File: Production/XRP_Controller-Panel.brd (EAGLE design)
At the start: 147.6 x 122.7 mm, 610 parts, among them J1 POWER_JACKPOWER_JACK_SLOT, J10 JST_6_PIN_VERTICAL, J11 JST_6_PIN_VERTICAL, J12 Vertical Qwiic Connector, J13 Vertical Qwiic Connector, J14 Vertical Qwiic Connector, J15 JST_6_PIN_VERTICAL, J18 Vertical Qwiic Connector, J19 Vertical Qwiic Connector, J2 JST_6_PIN_VERTICAL, J20 Vertical Qwiic Connector, J21 Vertical Qwiic Connector, J22 POWER_JACKPOWER_JACK_SLOT, J23 JST_6_PIN_VERTICAL, J24 JST_6_PIN_VERTICAL, J25 JST_6_PIN_VERTICAL, J26 JST_6_PIN_VERTICAL, J29 Vertical Qwiic Connector, J3 JST_6_PIN_VERTICAL, J30 Vertical Qwiic Connector, J31 Vertical Qwiic Connector, J32 Vertical Qwiic Connector, J33 POWER_JACKPOWER_JACK_SLOT, J34 JST_6_PIN_VERTICAL, J35 JST_6_PIN_VERTICAL, J36 JST_6_PIN_VERTICAL, J37 JST_6_PIN_VERTICAL, J4 JST_6_PIN_VERTICAL, J40 Vertical Qwiic Connector, J41 Vertical Qwiic Connector, J42 Vertical Qwiic Connector, J43 Vertical Qwiic Connector, J44 POWER_JACKPOWER_JACK_SLOT, J5 JST_6_PIN_VERTICAL, J6 JST_6_PIN_VERTICAL, J9 Vertical Qwiic Connector, Q12 20V/4.2A/52mΩ/1.4W, Q13 20V/4.2A/52mΩ/1.4W, Q15 20V/4.2A/52mΩ/1.4W, Q16 20V/4.2A/52mΩ/1.4W, Q19 20V/4.2A/52mΩ/1.4W, Q20 20V/4.2A/52mΩ/1.4W, Q22 20V/4.2A/52mΩ/1.4W, Q23 20V/4.2A/52mΩ/1.4W, Q26 20V/4.2A/52mΩ/1.4W, Q27 20V/4.2A/52mΩ/1.4W, Q3 20V/4.2A/52mΩ/1.4W, Q4 20V/4.2A/52mΩ/1.4W, Q5 20V/4.2A/52mΩ/1.4W, Q6 20V/4.2A/52mΩ/1.4W, Q8 20V/4.2A/52mΩ/1.4W, Q9 20V/4.2A/52mΩ/1.4W, U1 RPI_PICO_W, U10 AP63357, U11 LSM6DS0, U12 DRV8835, U13 DRV8835, U14 RPI_PICO_W, U15 AP63357, U16 LSM6DS0, U17 DRV8835, U18 DRV8835, U19 RPI_PICO_W, U2 AP63357, U20 AP63357, U3 LSM6DS0, U4 LSM6DS0, U5 DRV8835, U6 DRV8835, U7 DRV8835, U8 DRV8835, U9 RPI_PICO_W

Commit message: Add v09 panel files
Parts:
- removed C31, C34, C35, C36, C38, C42, C43, C44, C45, C48, C49, C50, C52, C56: 0.1uF, SparkFun-Capacitors:0603
- removed C32, C33, C46, C47: 100uF, SparkFun-Capacitors:PANASONIC_D
- removed C37, C51: 10uF, SparkFun-Capacitors:0805
- removed C39, C53: 47pF, SparkFun-Capacitors:0603
- removed C40, C41, C54, C55: 22uF, SparkFun-Capacitors:0805
- removed F3, F4: 16V/2.5A(5A TRIP), SparkFun-Fuses:1812
- removed FD10, FD11, FD12, FD13, FD14, FD15, FD16, FD9: FIDUCIAL1X2, SparkFun-Aesthetics:FIDUCIAL-1X2
- removed H10, H11, H12, H13, H14, H15, H16, H9: STAND-OFF, SparkFun-Hardware:STAND-OFF
- removed I2C2, I2C3: JUMPER-SMT_3_2-NC_TRACE_SILK, SparkFun-Jumpers:SMT-JUMPER_3_2-NC_TRACE_SILK
- removed IMU_ADR2, IMU_ADR3, USB_POW, USB_POW1, USB_POW2, USB_POW3: JUMPER-SMT_2_NO_SILK, SparkFun-Jumpers:SMT-JUMPER_2_NO_SILK
- removed J23, J24, J25, J26, J34, J35, J36, J37: JST_6_PIN_VERTICAL, SparkFun-Connectors:JST-6-SMD-VERT-1.0MM
- removed J27, J28, J38, J39: (no value), SparkFun-Connectors:1X03_NO_SILK
- removed J29, J30, J31, J32, J40, J41, J42, J43: Vertical Qwiic Connector, SparkFun-Connectors:JST04_1MM_VERT
- removed J33, J44: POWER_JACKPOWER_JACK_SLOT, SparkFun-Connectors:POWER_JACK_PTH_SLOT
- removed L3, L4: 6.8UH, Buck5V:07A7_6U8H
- removed LOGO10, LOGO14: QWIIC_LOGO_5MM, SparkFun-Aesthetics:QWIIC_5MM
- removed LOGO11, LOGO12, LOGO15, LOGO16, LOGO7, LOGO8: SFE_LOGO_NAME_FLAME.1_INCH, SparkFun-Aesthetics:SFE_LOGO_NAME_FLAME_.1
- removed LOGO13, LOGO9: OSHW-LOGOS, SparkFun-Aesthetics:OSHW-LOGO-S
- removed MOT_MODE_L1, MOT_MODE_L3, MOT_MODE_R1, MOT_MODE_R3, PWR, PWR1, PWR2, PWR3: JUMPER-SMT_2_NC_TRACE_SILK, SparkFun-Jumpers:SMT-JUMPER_2_NC_TRACE_SILK
- removed Q15, Q16, Q19, Q20, Q22, Q23, Q26, Q27: 20V/4.2A/52mΩ/1.4W, SparkFun-DiscreteSemi:SOT23-3
- removed Q17, Q18, Q21, Q24, Q25, Q28: (no value), SparkFun-DiscreteSemi:SOT363_PHILIPS
- removed R41, R46, R49, R50, R53, R54, R55: 100k, SparkFun-Resistors:0603
- removed R42, R51, R52, R56: 1M, SparkFun-Resistors:0603
- removed R43: 1k, SparkFun-Resistors:0603
- removed R44, R45: 2.2k, SparkFun-Resistors:0603
- removed R47: 180k, SparkFun-Resistors:0603
- removed R48: 33k, SparkFun-Resistors:0603
- removed RESET2, RESET3: MOMENTARY-SWITCH-SPST-SMD-4.6X2.8MM, SparkFun-Switches:TACTILE_SWITCH_SMD_4.6X2.8MM
- removed S3, S4: (no value), SparkFun-Switches:SWITCH_SPST_SMD_A
- removed U$193, U$267: (no value), output:#I2C#0
- removed U$194, U$268: (no value), output:ON0
- removed U$195, U$269: (no value), output:OFF0
- removed U$196, U$270: (no value), output:X0
- removed U$197, U$271: (no value), output:Y0
- removed U$198, U$272: (no value), output:Z0
- removed U$199, U$273: (no value), output:#IMU_ADR#0
- removed U$200, U$274: (no value), output:#USB_POW#0
- removed U$201, U$275: (no value), output:#MOT_MODE_R#0
- removed U$202, U$276: (no value), output:#MOT_MODE_L#0
- removed U$203, U$277: (no value), output:#PWR_LED#0
- removed U$204, U$206, U$278, U$280: (no value), output:XRP_ROBOT0
- removed U$205, U$207, U$279, U$281: (no value), output:CONTROLLER0
- removed U$208, U$282: (no value), output:#RANGE#0
- removed U$209, U$283: (no value), output:#LINE#0
- removed U$210, U$284: (no value), output:#MOTOR_L#0
- removed U$211, U$285: (no value), output:#MOTOR_3#0
- removed U$212, U$286: (no value), output:#SERVO_1#0
- removed U$213, U$287: (no value), output:#MOTOR_R#0
- removed U$214, U$288: (no value), output:#MOTOR_4#0
- removed U$215, U$289: (no value), output:#SERVO_2#0
- removed U$216, U$290: (no value), output:#11V_MAX###0
- removed U$217, U$291: (no value), output:#MLP#0
- removed U$218, U$292: (no value), output:#MLN#0
- removed U$219, U$293: (no value), output:#M3N#0
- removed U$220, U$294: (no value), output:#M3P#0
- removed U$221, U$295: (no value), output:#MRN#0
- removed U$222, U$296: (no value), output:#MRP#0
- removed U$223: (no value), output:#POWER#0
- removed U$224: (no value), output:PWR0
- removed U$225: (no value), output:RESET0
- removed U$226: (no value), output:#CONN4#0
- removed U$227, U$233, U$257, U$259, U$261: (no value), output:#GND#0
- removed U$228, U$234, U$258, U$260: (no value), output:#3V3#0
- removed U$229: (no value), output:#IO0#0
- removed U$230: (no value), output:#IO1#0
- removed U$231: (no value), output:#IO5#0
- removed U$232: (no value), output:#IO4#0
- removed U$235: (no value), output:#IO8#0
- removed U$236: (no value), output:#IO9#0
- removed U$237, U$239, U$247, U$249, U$264: (no value), output:#GND#10
- removed U$238, U$240, U$248, U$250: (no value), output:#3V3#4
- removed U$241: (no value), output:#IO12#0
- removed U$242: (no value), output:#IO13#0
- removed U$243: (no value), output:#M4P#0
- removed U$244: (no value), output:#M4N#0
- removed U$245: (no value), output:#IO27#0
- removed U$246: (no value), output:#IO28#0
- removed U$251: (no value), output:#IO26#0
- removed U$252: (no value), output:#IO22#0
- removed U$253: (no value), output:#IO18#0
- removed U$254: (no value), output:#IO19#0
- removed U$255: (no value), output:#IO20#0
- removed U$256: (no value), output:#IO21#0
- removed U$262: (no value), output:#5V#0
- removed U$263: (no value), output:#IO16#0
- removed U$265: (no value), output:#IO17#0
- removed U$266: (no value), output:#5V#18
- removed U11, U16: LSM6DS0, SparkFun-Sensors:LGA14L
- removed U12, U13, U17, U18: DRV8835, SparkFun-IC-Special-Function:WSON-12
- removed U14, U19: RPI_PICO_W, RPI_PICO_W:RPI_PICO_W
- removed U15, U20: AP63357, Buck5V:V-DFN3020-13
- added MOT_PWR, MOT_PWR1, SYS_PWR, SYS_PWR1, USER_BTN, USER_BTN1, VIN_MEAS, VIN_MEAS1, VUSB, VUSB1: JUMPER-SMT_2_NC_TRACE_SILK, SparkFun-Jumpers:SMT-JUMPER_2_NC_TRACE_SILK
- added TP13, TP14, TP15, TP16, TP17, TP18, TP19, TP20, TP21, TP22, TP23, TP24, TP25, TP26, TP27, TP28, TP29, TP30, TP31, TP32, TP33, TP34, TP35, TP36, TP37, TP38, TP39, TP40, TP41, TP42, TP43, TP44, TP45, TP46, TP47, TP48, TP49, TP50, TP51, TP52, TP53, TP54, TP55, TP56, TP57, TP58, TP59, TP60, TP61, TP62, TP63, TP64, TP65, TP66, TP67, TP68, TP69, TP70, TP71, TP72, TP73, TP74, TP75, TP76, TP77, TP78: TEST-POINT3X5, SparkFun-Connectors:PAD.03X.05
- added USER, USER1: MOMENTARY-SWITCH-SPST-SMD-4.6X2.8MM, SparkFun-Switches:TACTILE_SWITCH_SMD_4.6X2.8MM
- C18: value 100uF -> 0.1uF; device SparkFun-Capacitors:PANASONIC_D -> SparkFun-Capacitors:0603
- C20: value 0.1uF -> 100uF; device SparkFun-Capacitors:0603 -> SparkFun-Capacitors:PANASONIC_D
- C23: value 10uF -> 0.1uF; device SparkFun-Capacitors:0805 -> SparkFun-Capacitors:0603
- C24: value 0.1uF -> 10uF; device SparkFun-Capacitors:0603 -> SparkFun-Capacitors:0805
- C25: value 47pF -> 0.1uF
- C26: value 22uF -> 47pF; device SparkFun-Capacitors:0805 -> SparkFun-Capacitors:0603
- C28: value 0.1uF -> 22uF; device SparkFun-Capacitors:0603 -> SparkFun-Capacitors:0805
- IMU_ADR, IMU_ADR1: value JUMPER-SMT_2_NO_SILK -> JUMPER-SMT_2_NC_TRACE_SILK; device SparkFun-Jumpers:SMT-JUMPER_2_NO_SILK -> SparkFun-Jumpers:SMT-JUMPER_2_NC_TRACE_SILK
- J16, J17, J7, J8: device SparkFun-Connectors:1X03_NO_SILK -> SparkFun-Connectors:1X03_LOCK_NO_SILK
- LOGO2: value QWIIC_LOGO_5MM -> OSHW-LOGOS; device SparkFun-Aesthetics:QWIIC_5MM -> SparkFun-Aesthetics:OSHW-LOGO-S
- LOGO3: value SFE_LOGO_NAME_FLAME.1_INCH -> SFE_LOGO_NAME_FLAME.3_INCH; device SparkFun-Aesthetics:SFE_LOGO_NAME_FLAME_.1 -> SparkFun-Aesthetics:SFE_LOGO_NAME_FLAME_.3
- LOGO5: value OSHW-LOGOS -> SFE_LOGO_NAME_FLAME.3_INCH; device SparkFun-Aesthetics:OSHW-LOGO-S -> SparkFun-Aesthetics:SFE_LOGO_NAME_FLAME_.3
- LOGO6: value QWIIC_LOGO_5MM -> SFE_LOGO_NAME_FLAME.1_INCH; device SparkFun-Aesthetics:QWIIC_5MM -> SparkFun-Aesthetics:SFE_LOGO_NAME_FLAME_.1
- R15: value 1k -> 33k
- R16, R17, R31: value 2.2k -> 100k
- R18, R39: value 100k -> 10; device SparkFun-Resistors:0603 -> SparkFun-Resistors:1206
- R19: value 180k -> 10; device SparkFun-Resistors:0603 -> SparkFun-Resistors:1206
- R20: value 33k -> 10k
- R21: value 100k -> 4.7k
- R22: value 100k -> 2.2k
- R23: value 1M -> 2.2k
- R24, R28, R37: value 1M -> 100k
- R25: value 100k -> 180k
- R26, R36: value 100k -> 33k
- R29: value 1k -> 1M
- R30: value 2.2k -> 1M
- R33: value 180k -> 100k
- R34: value 33k -> 1M
- R38: value 1M -> 10; device SparkFun-Resistors:0603 -> SparkFun-Resistors:1206
- R40: value 100k -> 10k
- R8: value 1k -> 4.7k
- U$100: device output:#3V3#4 -> output:#GND#0
- U$101: device output:#GND#10 -> output:#3V3#0
- U$102: device output:#3V3#4 -> output:#IO0#0
- U$103: device output:#IO26#0 -> output:#IO1#0
- U$104: device output:#IO22#0 -> output:#IO5#0
- U$105: device output:#IO18#0 -> output:#IO4#0
- U$106: device output:#IO19#0 -> output:#GND#0
- U$107: device output:#IO20#0 -> output:#3V3#0
- U$108: device output:#IO21#0 -> output:#IO8#0
- U$109: device output:#GND#0 -> output:#IO9#0
- U$110, U$112: device output:#3V3#0 -> output:#GND#10
- U$111, U$113: device output:#GND#0 -> output:#3V3#4
- U$114: device output:#5V#0 -> output:#IO12#0
- U$115: device output:#IO16#0 -> output:#IO13#0
- U$116: device output:#GND#10 -> output:#M4P#0
- U$117: device output:#IO17#0 -> output:#M4N#0
- U$118: device output:#5V#18 -> output:#IO27#0
- U$119: device output:#I2C#0 -> output:#IO28#0
- U$120: device output:ON0 -> output:#GND#10
- U$121: device output:OFF0 -> output:#3V3#4
- U$122: device output:X0 -> output:#GND#10
- U$123: device output:Y0 -> output:#3V3#4
- U$124: device output:Z0 -> output:#IO26#0
- U$125: device output:#IMU_ADR#0 -> output:#IO22#0
- U$126: device output:#USB_POW#0 -> output:#IO18#0
- U$127: device output:#MOT_MODE_R#0 -> output:#IO19#0
- U$128: device output:#MOT_MODE_L#0 -> output:#IO20#0
- U$129: device output:#PWR_LED#0 -> output:#IO21#0
- U$13: device output:#CONN4#0 -> output:#VIN_MEAS#0
- U$130, U$132: device output:XRP_ROBOT0 -> output:#GND#0
- U$131, U$133: device output:CONTROLLER0 -> output:#3V3#0
- U$134: device output:#RANGE#0 -> output:#GND#0
- U$135: device output:#LINE#0 -> output:#5V#0
- U$136: device output:#MOTOR_L#0 -> output:#IO16#0
- U$137: device output:#MOTOR_3#0 -> output:#GND#10
- U$138: device output:#SERVO_1#0 -> output:#IO17#0
- U$139: device output:#MOTOR_R#0 -> output:#5V#18
- U$140: device output:#MOTOR_4#0 -> output:#I2C#0
- U$141: device output:#SERVO_2#0 -> output:ON0
- U$142: device output:#11V_MAX###0 -> output:OFF0
- U$143: device output:#MLP#0 -> output:X0
- U$144: device output:#MLN#0 -> output:Y0
- U$145: device output:#M3N#0 -> output:Z0
- U$146: device output:#M3P#0 -> output:#IMU_ADR#0
- U$147: device output:#MRN#0 -> output:#LINE#0
- U$148: device output:#MRP#0 -> output:#MOTOR_L#0
- U$149: device output:#POWER#0 -> output:#MOTOR_3#0
- U$150: device output:PWR0 -> output:#SERVO_1#0
- U$151: device output:RESET0 -> output:#MOTOR_R#0
- U$152: device output:#CONN4#0 -> output:#MOTOR_4#0
- U$153: device output:#GND#0 -> output:#SERVO_2#0
- U$154: device output:#3V3#0 -> output:#11V_MAX###0
- U$155: device output:#IO0#0 -> output:#MLP#0
- U$156: device output:#IO1#0 -> output:#MLN#0
- U$157: device output:#IO5#0 -> output:#M3N#0
- U$158: device output:#IO4#0 -> output:#M3P#0
- U$159: device output:#GND#0 -> output:#MRN#0
- U$160: device output:#3V3#0 -> output:#MRP#0
- U$161: device output:#IO8#0 -> output:#5V_#0
- U$162: device output:#IO9#0 -> output:#GND_#0
- U$163: device output:#GND#10 -> output:#IO16_#0
- U$164: device output:#3V3#4 -> output:#_GND#0
- U$165: device output:#GND#10 -> output:#_5V#0
- U$166: device output:#3V3#4 -> output:#_IO17#0
- U$167: device output:#IO12#0 -> SparkFun-Aesthetics:POLARITY_MARKING_CENTER_POSITIVE#JPG
- U$168: device output:#IO13#0 -> output:X0
- U$169: device output:#M4P#0 -> output:Y0
- U$170: device output:#M4N#0 -> output:Z0
- U$171: device output:#IO27#0 -> output:#EXTRA#0
- U$172: device output:#IO28#0 -> output:#VIN_MEAS#0
- U$173: device output:#GND#10 -> output:USER0
- U$174: device output:#3V3#4 -> output:#USER_BTN#0
- U$175: device output:#GND#10 -> output:0X6B0
- U$176: device output:#3V3#4 -> output:0X6A0
- U$177: device output:#IO26#0 -> output:OPEN#0
- U$178: device output:#IO22#0 -> output:CLOSED#0
- U$179: device output:#IO18#0 -> XRP_LOGOS:XRP_FULL_LOGO
- U$180: device output:#IO19#0 -> output:#VUSB#0
- U$181: device output:#IO20#0 -> XRP_LOGOS:XRP_LOGO
- U$182: device output:#IO21#0 -> output:IO220
- U$183: device output:#GND#0 -> output:#RANGE#0
- U$184: device output:#3V3#0 -> output:#MOT_MODE_R#4#0
- U$185: device output:#GND#0 -> output:#MOT_MODE_L#3#0
- U$186: device output:#3V3#0 -> output:SYS0
- U$187: device output:#GND#0 -> output:MOT0
- U$188: device output:#5V#0 -> output:#MOT#0
- U$189: device output:#IO16#0 -> output:#SYS#0
- U$190: device output:#GND#10 -> output:#PWR#0
- U$191: device output:#IO17#0 -> XRP_COMPONENTS:OPENSTEM_LOGO
- U$192: value (none) -> QWIIC_LOGO; device output:#5V#18 -> XRP_COMPONENTS:QWIIC_INVERTED
- U$26: device output:#POWER#0 -> output:#GND_#0
- U$27: device output:PWR0 -> output:#5V_#0
- U$61: device output:RESET0 -> output:#IO16_#0
- U$65: device output:#USB_POW#0 -> XRP_LOGOS:XRP_LOGO
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- renumbered MOT_MODE_L to MOT_MODE_L/3, MOT_MODE_L2 to MOT_MODE_L/1, MOT_MODE_R to MOT_MODE_R/4, MOT_MODE_R2 to MOT_MODE_R/1
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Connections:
- net N$12 renamed V_SYS
- net N$17 renamed V_POW
- removed net !POW_EN!2: R40.1, S3.2
- removed net !POW_EN!3: R54.1, S4.2
- removed net !RP_RESET!2: C42.1, RESET2.3, RESET2.4, U14.30
- removed net !RP_RESET!3: C56.1, RESET3.3, RESET3.4, U19.30
- removed net 3.3V2: C29.1, C30.1, C31.1, C34.1, D3.A, I2C2.2, J23.3, J24.3, J25.3, J26.3, J29.2, J30.2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
- removed net 3.3V3: C43.1, C44.1, C45.1, C48.1, D4.A, I2C3.2, J34.3, J35.3, J36.3, J37.3, J40.2, J41.2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
- removed net 5V2: C39.1, C40.1, C41.1, J27.2, J28.2, L3.P$2, Q20.3, Q21.1, R33.2
- removed net 5V3: C53.1, C54.1, C55.1, J38.2, J39.2, L4.P$2, Q27.3, Q28.1, R47.2
- removed net 5V_EN2: TP7.1, U15.P$2
- removed net 5V_EN3: TP10.1, U20.P$2
- removed net 5V_PG2: TP8.1, U15.P$5
- removed net 5V_PG3: TP11.1, U20.P$5
- removed net BOOTSEL2: TP9.1, U14.46
- removed net BOOTSEL3: TP12.1, U19.46
- removed net FB2: C39.2, R33.1, R34.2, U15.P$3
- removed net FB3: C53.2, R47.1, R48.2, U20.P$3
- removed net GND2: C29.2, C30.2, C31.2, C32.-, C33.-, C34.2, C35.2, C36.2, C37.2, C40.2, C41.2, C42.2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
- removed net GND3: C43.2, C44.2, C45.2, C46.-, C47.-, C48.2, C49.2, C50.2, C51.2, C54.2, C55.2, C56.2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
- removed net MOT_3_N2: J23.2, U12.5
- removed net MOT_3_N3: J34.2, U17.5
- removed net MOT_3_P2: J23.1, U12.4
- removed net MOT_3_P3: J34.1, U17.4
- removed net MOT_4_N2: J26.2, U13.3
- removed net MOT_4_N3: J37.2, U18.3
- removed net MOT_4_P2: J26.1, U13.2
- removed net MOT_4_P3: J37.1, U18.2
- removed net MOT_L_N2: J24.2, U12.3
- removed net MOT_L_N3: J35.2, U17.3
- removed net MOT_L_P2: J24.1, U12.2
- removed net MOT_L_P3: J35.1, U17.2
- removed net MOT_R_N2: J25.2, U13.5
- removed net MOT_R_N3: J36.2, U18.5
- removed net MOT_R_P2: J25.1, U13.4
- removed net MOT_R_P3: J36.1, U18.4
- removed net N$36 (its old number): Q13.2, Q14.4, U9.39
- removed net N$45: I2C2.1, R31.1
- removed net N$46: C38.1, U15.P$6
- removed net N$47: Q17.2, Q17.5, Q17.6, R35.2
- removed net N$48: Q15.1, Q17.3, R37.2
- removed net N$49: Q18.2, Q18.5, Q18.6, R36.2
- removed net N$50: Q16.1, Q18.3, R38.2
- removed net N$51: Q16.3, Q18.1, USB_POW2.2
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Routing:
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- added copper zone on layer 1, net V_POW
- added copper zone on layer 1, net V_POW1
- removed copper zone on layer 1, net 3.3V2
- removed copper zone on layer 1, net 3.3V3
- removed copper zone on layer 1, net 5V2
- removed copper zone on layer 16, net 5V2
- removed copper zone on layer 1, net 5V3
- removed copper zone on layer 16, net 5V3
- removed copper zone on layer 1, net FB2
- removed copper zone on layer 1, net FB3
- removed copper zone on layer 1, net GND2
- removed copper zone on layer 16, net GND2
- removed copper zone on layer 1, net GND3
- removed copper zone on layer 16, net GND3
- removed copper zone on layer 1, net SW2
- removed copper zone on layer 1, net SW3
- removed copper zone on layer 1, net VIN2
- removed copper zone on layer 1, net VIN3
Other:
- board size 147.6 x 122.7 mm -> 83.6 x 122.7 mm
- board text added: "v09"
- board text removed: "v01"

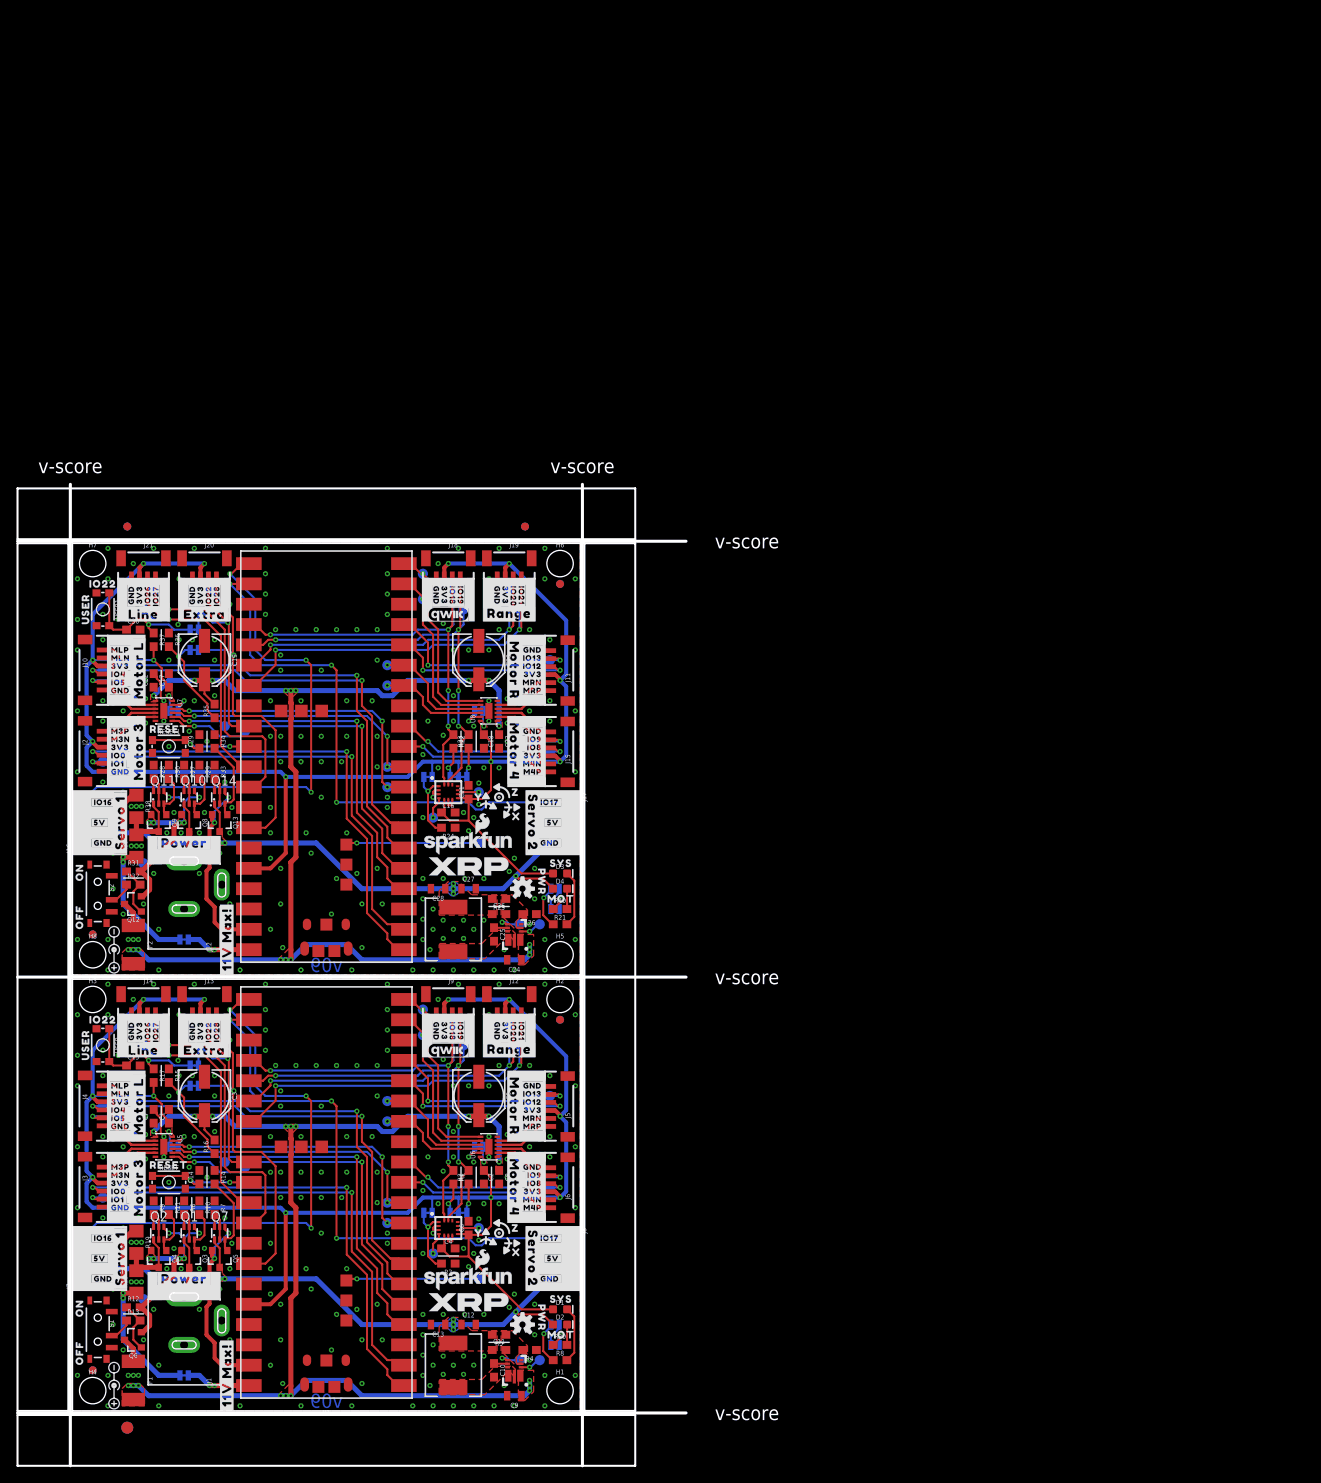
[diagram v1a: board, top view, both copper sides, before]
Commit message: Add v10 panel files
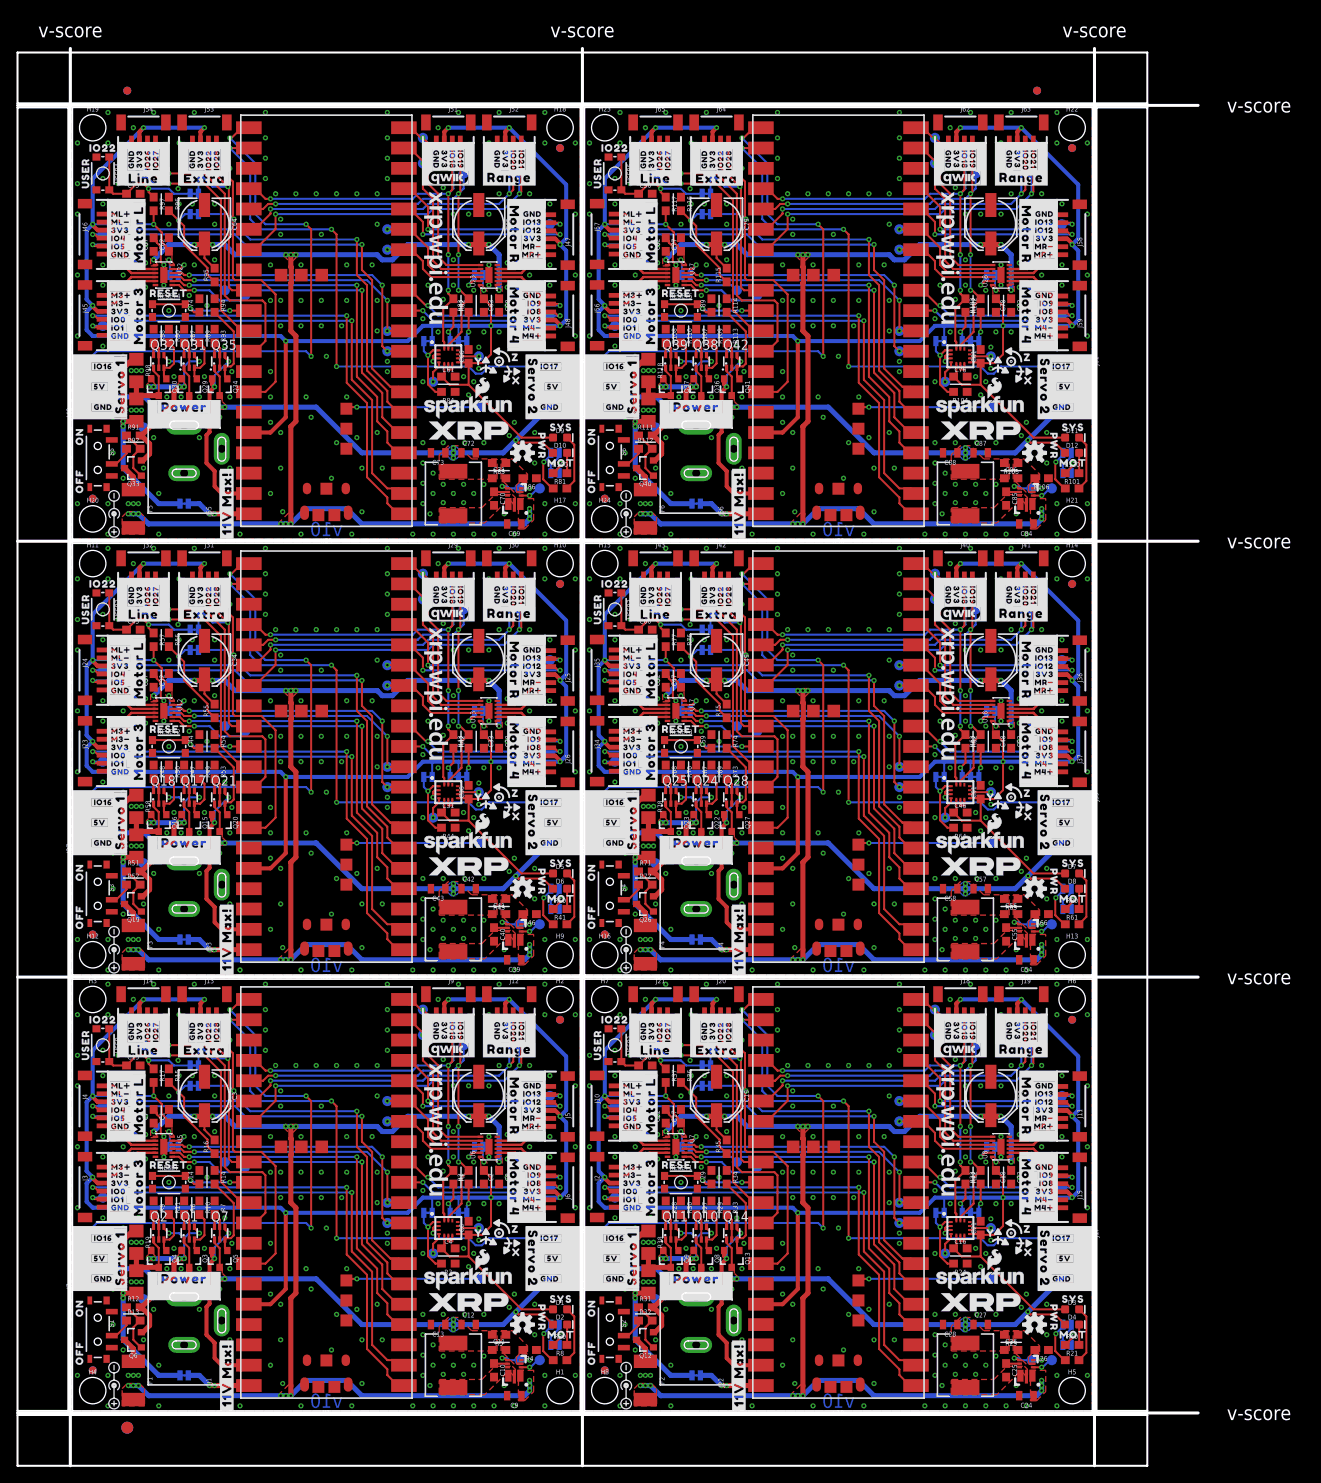
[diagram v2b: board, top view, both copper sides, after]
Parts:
- added C31, C32, C33, C36, C37, C38, C40, C44, C45, C46, C47, C48, C51, C52, C53, C55, C59, C60, C61, C62, C63, C66, C67, C68, C70, C74, C75, C76, C77, C78, C81, C82, C83, C85, C89, C90: 0.1uF, SparkFun-Capacitors:0603
- added C34, C35, C49, C50, C64, C65, C79, C80: 100uF, SparkFun-Capacitors:PANASONIC_D
- added C39, C54, C69, C84: 10uF, SparkFun-Capacitors:0805
- added C41, C56, C71, C86: 47pF, SparkFun-Capacitors:0603
- added C42, C43, C57, C58, C72, C73, C87, C88: 22uF, SparkFun-Capacitors:0805
- added D10, D11, D12, D5, D6, D7, D8, D9: Red, SparkFun-LED:LED-0603
- added F3, F4, F5, F6: 16V/2.5A(5A TRIP), SparkFun-Fuses:1812
- added FD10, FD11, FD12, FD13, FD14, FD15, FD16, FD17, FD18, FD19, FD20, FD21, FD22, FD23, FD24, FD9: FIDUCIAL1X2, SparkFun-Aesthetics:FIDUCIAL-1X2
- added H10, H11, H12, H13, H14, H15, H16, H17, H18, H19, H20, H21, H22, H23, H24, H9: STAND-OFF, SparkFun-Hardware:STAND-OFF
- added I2C2, I2C3, I2C4, I2C5: JUMPER-SMT_3_2-NC_TRACE_SILK, SparkFun-Jumpers:SMT-JUMPER_3_2-NC_TRACE_SILK
- added IMU_ADR2, IMU_ADR3, IMU_ADR4, IMU_ADR5, MOT_MODE_L/2, MOT_MODE_L/4, MOT_MODE_L/5, MOT_MODE_L/6, MOT_MODE_R/2, MOT_MODE_R/3, MOT_MODE_R/5, MOT_MODE_R/6, MOT_PWR2, MOT_PWR3, MOT_PWR4, MOT_PWR5, SYS_PWR2, SYS_PWR3, SYS_PWR4, SYS_PWR5, USER_BTN2, USER_BTN3, USER_BTN4, USER_BTN5, VIN_MEAS2, VIN_MEAS3, VIN_MEAS4, VIN_MEAS5, VUSB2, VUSB3, VUSB4, VUSB5: JUMPER-SMT_2_NC_TRACE_SILK, SparkFun-Jumpers:SMT-JUMPER_2_NC_TRACE_SILK
- added J23, J24, J25, J26, J34, J35, J36, J37, J45, J46, J47, J48, J56, J57, J58, J59: JST_6_PIN_VERTICAL, SparkFun-Connectors:JST-6-SMD-VERT-1.0MM
- added J27, J28, J38, J39, J49, J50, J60, J61: (no value), SparkFun-Connectors:1X03_LOCK_NO_SILK
- added J29, J30, J31, J32, J40, J41, J42, J43, J51, J52, J53, J54, J62, J63, J64, J65: Vertical Qwiic Connector, SparkFun-Connectors:JST04_1MM_VERT
- added J33, J44, J55, J66: POWER_JACKPOWER_JACK_SLOT, SparkFun-Connectors:POWER_JACK_PTH_SLOT
- added L3, L4, L5, L6: 6.8UH, Buck5V:07A7_6U8H
- added LOGO10, LOGO13, LOGO16, LOGO7: OSHW-LOGOS, SparkFun-Aesthetics:OSHW-LOGO-S
- added LOGO11, LOGO14, LOGO17, LOGO8: SFE_LOGO_NAME_FLAME.3_INCH, SparkFun-Aesthetics:SFE_LOGO_NAME_FLAME_.3
- added LOGO12, LOGO15, LOGO18, LOGO9: SFE_LOGO_NAME_FLAME.1_INCH, SparkFun-Aesthetics:SFE_LOGO_NAME_FLAME_.1
- added Q15, Q16, Q19, Q20, Q22, Q23, Q26, Q27, Q29, Q30, Q33, Q34, Q36, Q37, Q40, Q41: 20V/4.2A/52mΩ/1.4W, SparkFun-DiscreteSemi:SOT23-3
- added Q17, Q18, Q21, Q24, Q25, Q28, Q31, Q32, Q35, Q38, Q39, Q42: (no value), SparkFun-DiscreteSemi:SOT363_PHILIPS
- added R100, R120, R60, R80: 10k, SparkFun-Resistors:0603
- added R101, R41, R61, R81: 4.7k, SparkFun-Resistors:0603
- added R102, R103, R42, R43, R62, R63, R82, R83: 2.2k, SparkFun-Resistors:0603
- added R104, R107, R108, R111, R112, R113, R115, R117, R44, R47, R48, R51, R52, R53, R55, R57, R64, R67, R68, R71, R72, R73, R75, R77, R84, R87, R88, R91, R92, R93, R95, R97: 100k, SparkFun-Resistors:0603
- added R105, R45, R65, R85: 180k, SparkFun-Resistors:0603
- added R106, R116, R46, R56, R66, R76, R86, R96: 33k, SparkFun-Resistors:0603
- added R109, R110, R114, R49, R50, R54, R69, R70, R74, R89, R90, R94: 1M, SparkFun-Resistors:0603
- added R118, R119, R58, R59, R78, R79, R98, R99: 10, SparkFun-Resistors:1206
- added RESET2, RESET3, RESET4, RESET5, USER2, USER3, USER4, USER5: MOMENTARY-SWITCH-SPST-SMD-4.6X2.8MM, SparkFun-Switches:TACTILE_SWITCH_SMD_4.6X2.8MM
- added S3, S4, S5, S6: (no value), SparkFun-Switches:SWITCH_SPST_SMD_A
- added TP100, TP101, TP102, TP103, TP104, TP105, TP106, TP107, TP108, TP109, TP110, TP111, TP112, TP113, TP114, TP115, TP116, TP117, TP118, TP119, TP120, TP121, TP122, TP123, TP124, TP125, TP126, TP127, TP128, TP129, TP130, TP131, TP132, TP133, TP134, TP135, TP136, TP137, TP138, TP139, TP140, TP141, TP142, TP143, TP144, TP145, TP146, TP147, TP148, TP149, TP150, TP151, TP152, TP153, TP154, TP155, TP156, TP157, TP158, TP159, TP160, TP161, TP162, TP163, TP164, TP165, TP166, TP167, TP168, TP169, TP170, TP171, TP172, TP173, TP174, TP175, TP176, TP177, TP178, TP179, TP180, TP181, TP182, TP183, TP184, TP185, TP186, TP187, TP188, TP189, TP190, TP191, TP192, TP193, TP194, TP195, TP196, TP197, TP198, TP199, TP200, TP201, TP202, TP203, TP204, TP205, TP206, TP207, TP208, TP209, TP210, TP211, TP212, TP213, TP214, TP215, TP216, TP217, TP218, TP219, TP220, TP221, TP222, TP223, TP224, TP225, TP226, TP227, TP228, TP229, TP230, TP231, TP232, TP233, TP234, TP79, TP80, TP81, TP82, TP83, TP84, TP85, TP86, TP87, TP88, TP89, TP90, TP91, TP92, TP93, TP94, TP95, TP96, TP97, TP98, TP99: TEST-POINT3X5, SparkFun-Connectors:PAD.03X.05
- added U$193, U$290, U$387, U$484, U$581: (no value), output:#M4##0
- added U$194, U$291, U$388, U$485, U$582: (no value), output:#M4##5
- added U$195, U$292, U$389, U$486: (no value), output:#POWER#0
- added U$196, U$293, U$390, U$487: (no value), output:PWR0
- added U$197, U$294, U$391, U$488: (no value), output:RESET0
- added U$198, U$204, U$226, U$228, U$230, U$295, U$301, U$323, U$325, U$327, U$392, U$398, U$420, U$422, U$424, U$489, U$495, U$517, U$519, U$521: (no value), output:#GND#0
- added U$199, U$205, U$227, U$229, U$296, U$302, U$324, U$326, U$393, U$399, U$421, U$423, U$490, U$496, U$518, U$520: (no value), output:#3V3#0
- added U$200, U$297, U$394, U$491: (no value), output:#IO0#0
- added U$201, U$298, U$395, U$492: (no value), output:#IO1#0
- added U$202, U$299, U$396, U$493: (no value), output:#IO5#0
- added U$203, U$300, U$397, U$494: (no value), output:#IO4#0
- added U$206, U$303, U$400, U$497: (no value), output:#IO8#0
- added U$207, U$304, U$401, U$498: (no value), output:#IO9#0
- added U$208, U$210, U$216, U$218, U$233, U$305, U$307, U$313, U$315, U$330, U$402, U$404, U$410, U$412, U$427, U$499, U$501, U$507, U$509, U$524: (no value), output:#GND#10
- added U$209, U$211, U$217, U$219, U$306, U$308, U$314, U$316, U$403, U$405, U$411, U$413, U$500, U$502, U$508, U$510: (no value), output:#3V3#4
- added U$212, U$309, U$406, U$503: (no value), output:#IO12#0
- added U$213, U$310, U$407, U$504: (no value), output:#IO13#0
- added U$214, U$311, U$408, U$505: (no value), output:#IO27#0
- added U$215, U$312, U$409, U$506: (no value), output:#IO28#0
- added U$220, U$317, U$414, U$511: (no value), output:#IO26#0
- added U$221, U$318, U$415, U$512: (no value), output:#IO22#0
- added U$222, U$319, U$416, U$513: (no value), output:#IO18#0
- added U$223, U$320, U$417, U$514: (no value), output:#IO19#0
- added U$224, U$321, U$418, U$515: (no value), output:#IO20#0
- added U$225, U$322, U$419, U$516: (no value), output:#IO21#0
- added U$231, U$328, U$425, U$522: (no value), output:#5V#0
- added U$232, U$329, U$426, U$523: (no value), output:#IO16#0
- added U$234, U$331, U$428, U$525: (no value), output:#IO17#0
- added U$235, U$332, U$429, U$526: (no value), output:#5V#18
- added U$236, U$333, U$430, U$527: (no value), output:#I2C#0
- added U$237, U$334, U$431, U$528: (no value), output:ON0
- added U$238, U$335, U$432, U$529: (no value), output:OFF0
- added U$239, U$258, U$336, U$355, U$433, U$452, U$530, U$549: (no value), output:X0
- added U$240, U$259, U$337, U$356, U$434, U$453, U$531, U$550: (no value), output:Y0
- added U$241, U$260, U$338, U$357, U$435, U$454, U$532, U$551: (no value), output:Z0
- added U$242, U$339, U$436, U$533: (no value), output:#IMU_ADR#0
- added U$243, U$340, U$437, U$534: (no value), output:#LINE#0
- added U$244, U$341, U$438, U$535: (no value), output:#MOTOR_L#0
- added U$245, U$342, U$439, U$536: (no value), output:#MOTOR_3#0
- added U$246, U$343, U$440, U$537: (no value), output:#SERVO_1#0
- added U$247, U$344, U$441, U$538: (no value), output:#MOTOR_R#0
- added U$248, U$345, U$442, U$539: (no value), output:#MOTOR_4#0
- added U$249, U$346, U$443, U$540: (no value), output:#SERVO_2#0
- added U$250, U$347, U$444, U$541: (no value), output:#11V_MAX###0
- added U$251, U$348, U$445, U$542: (no value), output:#5V_#0
- added U$252, U$349, U$446, U$543: (no value), output:#GND_#0
- added U$253, U$350, U$447, U$544: (no value), output:#IO16_#0
- added U$254, U$351, U$448, U$545: (no value), output:#_GND#0
- added U$255, U$352, U$449, U$546: (no value), output:#_5V#0
- added U$256, U$353, U$450, U$547: (no value), output:#_IO17#0
- added U$257, U$354, U$451, U$548: (no value), SparkFun-Aesthetics:POLARITY_MARKING_CENTER_POSITIVE#JPG
- added U$261, U$358, U$455, U$552: (no value), output:#EXTRA#0
- added U$262, U$359, U$456, U$553: (no value), output:#VIN_MEAS#0
- added U$263, U$360, U$457, U$554: (no value), output:USER0
- added U$264, U$361, U$458, U$555: (no value), output:#USER_BTN#0
- added U$265, U$362, U$459, U$556: (no value), output:0X6B0
- added U$266, U$363, U$460, U$557: (no value), output:0X6A0
- added U$267, U$364, U$461, U$558: (no value), output:OPEN#0
- added U$268, U$365, U$462, U$559: (no value), output:CLOSED#0
- added U$269, U$366, U$463, U$560: (no value), XRP_LOGOS:XRP_FULL_LOGO
- added U$270, U$367, U$464, U$561: (no value), output:#VUSB#0
- added U$271, U$368, U$465, U$562: (no value), XRP_LOGOS:XRP_LOGO
- added U$272, U$369, U$466, U$563: (no value), output:IO220
- added U$273, U$370, U$467, U$564: (no value), output:#RANGE#0
- added U$274, U$371, U$468, U$565: (no value), output:#MOT_MODE_R#4#0
- added U$275, U$372, U$469, U$566: (no value), output:#MOT_MODE_L#3#0
- added U$276, U$373, U$470, U$567: (no value), output:SYS0
- added U$277, U$374, U$471, U$568: (no value), output:MOT0
- added U$278, U$375, U$472, U$569: (no value), output:#MOT#0
- added U$279, U$376, U$473, U$570: (no value), output:#SYS#0
- added U$280, U$377, U$474, U$571: (no value), output:#PWR#0
- added U$281, U$378, U$475, U$572: QWIIC_LOGO, XRP_COMPONENTS:QWIIC_INVERTED
- added U$282, U$379, U$476, U$573: (no value), XRP_COMPONENTS:XRP_URL_3MM
- added U$283, U$380, U$477, U$574: (no value), XRP_COMPONENTS:XRP_URL_5MM
- added U$284, U$381, U$478, U$575: (no value), output:#M3##0
- added U$285, U$382, U$479, U$576: (no value), output:#M3##4
- added U$286, U$383, U$480, U$577: (no value), output:#ML##0
- added U$287, U$384, U$481, U$578: (no value), output:#ML##1
- added U$288, U$385, U$482, U$579: (no value), output:#MR##0
- added U$289, U$386, U$483, U$580: (no value), output:#MR##1
- added U11, U16, U21, U26: LSM6DS0X, XRP_COMPONENTS:LGA14L
- added U12, U13, U17, U18, U22, U23, U27, U28: DRV8835, SparkFun-IC-Special-Function:WSON-12
- added U14, U19, U24, U29: AP63357, SparkFun-IC-Power:V-DFN3020-13
- added U15, U20, U25, U30: RPI_PICO_W_XRP, XRP_COMPONENTS:RPI_PICO_W
- U$100: device output:#GND#0 -> output:RESET0
- U$101, U$107, U$131, U$133: device output:#3V3#0 -> output:#GND#0
- U$102: device output:#IO0#0 -> output:#3V3#0
- U$103: device output:#IO1#0 -> output:#IO0#0
- U$104: device output:#IO5#0 -> output:#IO1#0
- U$105: device output:#IO4#0 -> output:#IO5#0
- U$106: device output:#GND#0 -> output:#IO4#0
- U$108: device output:#IO8#0 -> output:#3V3#0
- U$109: device output:#IO9#0 -> output:#IO8#0
- U$110: device output:#GND#10 -> output:#IO9#0
- U$111, U$113, U$121: device output:#3V3#4 -> output:#GND#10
- U$112, U$120, U$122: device output:#GND#10 -> output:#3V3#4
- U$114: device output:#IO12#0 -> output:#3V3#4
- U$115: device output:#IO13#0 -> output:#IO12#0
- U$116: device output:#M4P#0 -> output:#IO13#0
- U$117: device output:#M4N#0 -> output:#IO27#0
- U$118: device output:#IO27#0 -> output:#IO28#0
- U$119: device output:#IO28#0 -> output:#GND#10
- U$123: device output:#3V3#4 -> output:#IO26#0
- U$124: device output:#IO26#0 -> output:#IO22#0
- U$125: device output:#IO22#0 -> output:#IO18#0
- U$126: device output:#IO18#0 -> output:#IO19#0
- U$127: device output:#IO19#0 -> output:#IO20#0
- U$128: device output:#IO20#0 -> output:#IO21#0
- U$129: device output:#IO21#0 -> output:#GND#0
- U$130, U$132: device output:#GND#0 -> output:#3V3#0
- U$134: device output:#GND#0 -> output:#5V#0
- U$135: device output:#5V#0 -> output:#IO16#0
- U$136: device output:#IO16#0 -> output:#GND#10
- U$137: device output:#GND#10 -> output:#IO17#0
- U$138: device output:#IO17#0 -> output:#5V#18
- U$139: device output:#5V#18 -> output:#I2C#0
- U$14: device output:#MLN#0 -> output:#MR##1
- U$140: device output:#I2C#0 -> output:ON0
- U$141: device output:ON0 -> output:OFF0
- U$142: device output:OFF0 -> output:X0
- U$143: device output:X0 -> output:Y0
- U$144: device output:Y0 -> output:Z0
- U$145: device output:Z0 -> output:#IMU_ADR#0
- U$146: device output:#IMU_ADR#0 -> output:#LINE#0
- U$147: device output:#LINE#0 -> output:#MOTOR_L#0
- U$148: device output:#MOTOR_L#0 -> output:#MOTOR_3#0
- U$149: device output:#MOTOR_3#0 -> output:#SERVO_1#0
- U$150: device output:#SERVO_1#0 -> output:#MOTOR_R#0
- U$151: device output:#MOTOR_R#0 -> output:#MOTOR_4#0
- U$152: device output:#MOTOR_4#0 -> output:#SERVO_2#0
- U$153: device output:#SERVO_2#0 -> output:#11V_MAX###0
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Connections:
- net MOT_3_N renamed MOT_3-
- net MOT_3_N1 renamed MOT_3-1
- net MOT_3_P renamed MOT_3+
- net MOT_3_P1 renamed MOT_3+1
- net MOT_4_N renamed MOT_4-
- net MOT_4_N1 renamed MOT_4-1
- net MOT_4_P renamed MOT_4+
- net MOT_4_P1 renamed MOT_4+1
- net MOT_L_N renamed MOT_L-
- net MOT_L_N1 renamed MOT_L-1
- net MOT_L_P renamed MOT_L+
- net MOT_L_P1 renamed MOT_L+1
- net MOT_R_N renamed MOT_R-
- net MOT_R_N1 renamed MOT_R-1
- net MOT_R_P renamed MOT_R+
- net MOT_R_P1 renamed MOT_R+1
- new net !POW_EN!2: R52.1, S3.2
- new net !POW_EN!3: R72.1, S4.2
- new net !POW_EN!4: R92.1, S5.2
- new net !POW_EN!5: R112.1, S6.2
- new net !RP_RESET!2: C44.1, RESET2.3, RESET2.4, U15.30
- new net !RP_RESET!3: C59.1, RESET3.3, RESET3.4, U20.30
- new net !RP_RESET!4: C74.1, RESET4.3, RESET4.4, U25.30
- new net !RP_RESET!5: C89.1, RESET5.3, RESET5.4, U30.30
- new net 3.3V2: C31.1, C32.1, C33.1, C36.1, D5.A, I2C2.2, IMU_ADR2.2, J23.3, J24.3, J25.3, J26.3, J29.2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
- new net 3.3V3: C46.1, C47.1, C48.1, C51.1, D7.A, I2C3.2, IMU_ADR3.2, J34.3, J35.3, J36.3, J37.3, J40.2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
- new net 3.3V4: C61.1, C62.1, C63.1, C66.1, D9.A, I2C4.2, IMU_ADR4.2, J45.3, J46.3, J47.3, J48.3, J51.2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
- new net 3.3V5: C76.1, C77.1, C78.1, C81.1, D11.A, I2C5.2, IMU_ADR5.2, J56.3, J57.3, J58.3, J59.3, J62.2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
- new net 5V2: C41.1, C42.1, C43.1, D6.A, J27.2, J28.2, L3.P$2, Q20.3, Q21.1, R45.2
- new net 5V3: C56.1, C57.1, C58.1, D8.A, J38.2, J39.2, L4.P$2, Q27.3, Q28.1, R65.2
- new net 5V4: C71.1, C72.1, C73.1, D10.A, J49.2, J50.2, L5.P$2, Q34.3, Q35.1, R85.2
- new net 5V5: C86.1, C87.1, C88.1, D12.A, J60.2, J61.2, L6.P$2, Q41.3, Q42.1, R105.2
- new net 5V_EN2: TP112.1, U14.P$2
- new net 5V_EN3: TP151.1, U19.P$2
- new net 5V_EN4: TP190.1, U24.P$2
- new net 5V_EN5: TP229.1, U29.P$2
- new net 5V_PG2: TP113.1, U14.P$5
- new net 5V_PG3: TP152.1, U19.P$5
- new net 5V_PG4: TP191.1, U24.P$5
- new net 5V_PG5: TP230.1, U29.P$5
- new net BOOTSEL2: TP114.1, U15.46
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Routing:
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- added copper zone on layer 1, net 3.3V2
- added copper zone on layer 1, net 3.3V3
- added copper zone on layer 1, net 3.3V4
- added copper zone on layer 1, net 3.3V5
- added copper zone on layer 1, net 5V2
- added copper zone on layer 16, net 5V2
- added copper zone on layer 1, net 5V3
- added copper zone on layer 16, net 5V3
- added copper zone on layer 1, net 5V4
- added copper zone on layer 16, net 5V4
- added copper zone on layer 1, net 5V5
- added copper zone on layer 16, net 5V5
- added copper zone on layer 1, net FB2
- added copper zone on layer 1, net FB3
- added copper zone on layer 1, net FB4
- added copper zone on layer 1, net FB5
- added copper zone on layer 1, net GND2
- added copper zone on layer 16, net GND2
- added copper zone on layer 1, net GND3
- added copper zone on layer 16, net GND3
- added copper zone on layer 1, net GND4
- added copper zone on layer 16, net GND4
- added copper zone on layer 1, net GND5
- added copper zone on layer 16, net GND5
- added copper zone on layer 1, net SW2
- added copper zone on layer 1, net SW3
- added copper zone on layer 1, net SW4
- added copper zone on layer 1, net SW5
- added copper zone on layer 1, net VIN2
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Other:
- board size 83.6 x 122.7 mm -> 147.6 x 177.2 mm
- board text added: "v10"
- board text removed: "v09"
